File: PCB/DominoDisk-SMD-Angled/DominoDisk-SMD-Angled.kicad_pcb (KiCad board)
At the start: 4 copper layers, 45 x 35.2 mm, 29 parts, among them J1 Daisy port out, J2 ICSP_ISP6, J3 Daisy port in, J4 UART, K1 TF-104 MicroSD card holder, U1 PC817C-S, U2 ATmega328P-AU, U3 TXB0104PWR level shifter, U4 SE5218ALG voltage regulator, Y1 CSTNE16M0V530000R0 Resonator

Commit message: Angled version
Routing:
- net GND: track 44.2 -> 45.2 mm

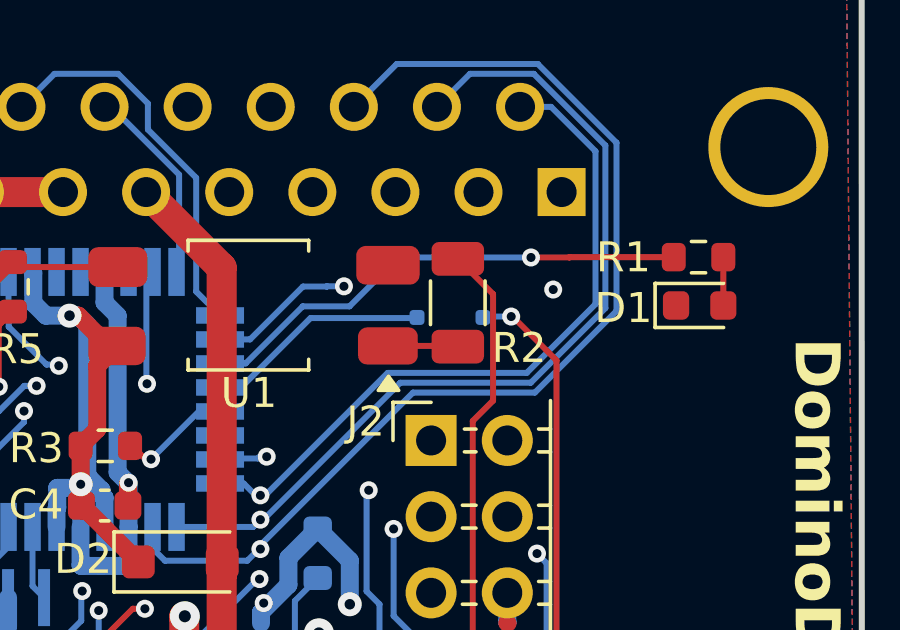
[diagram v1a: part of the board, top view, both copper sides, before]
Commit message: Move to bigger pads for diodes
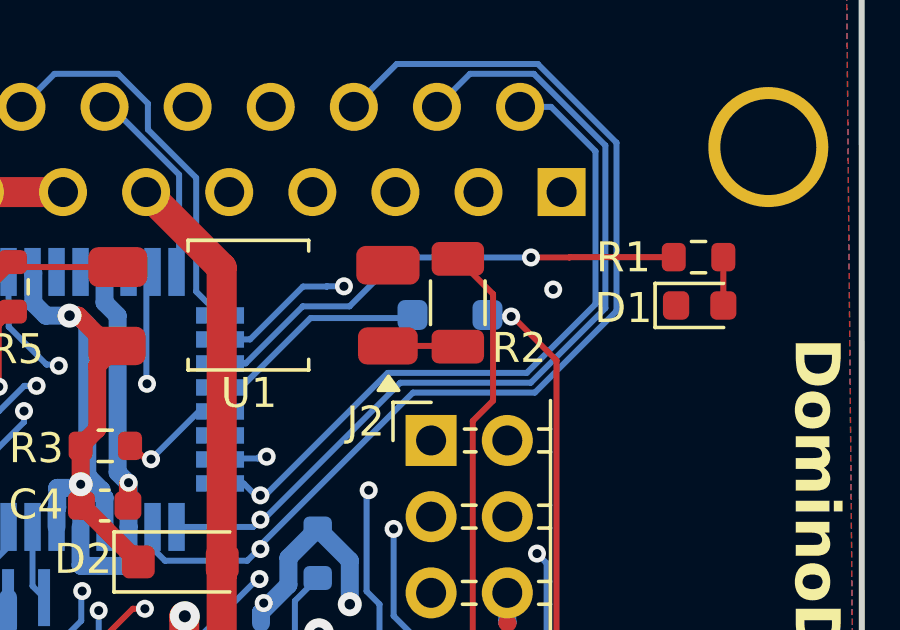
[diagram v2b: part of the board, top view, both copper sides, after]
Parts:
- D3: footprint Diode_SMD:D_SOD-323F -> Diode_SMD:D_SOD-323_HandSoldering
- moved D3 0.08 mm to (130.6, 51.6)
